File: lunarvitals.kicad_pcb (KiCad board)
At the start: 2 copper layers, 48.5 x 35 mm, 42 parts, among them J1 ConductiveCord, J2 MPU6050, J3 SEN11574, J4 MAX30102, J5 USB_C_Receptacle_PowerOnly_6P, J6 Battery, J7 Conn_01x07, Q1 FS8205, SW1 SW_SPDT, U1 NRF52840-DONGLE, U3 AP2112K-3.3, U4 TP4056, U5 MLX90614ESF-AAA-000-TU, U6 DW01A

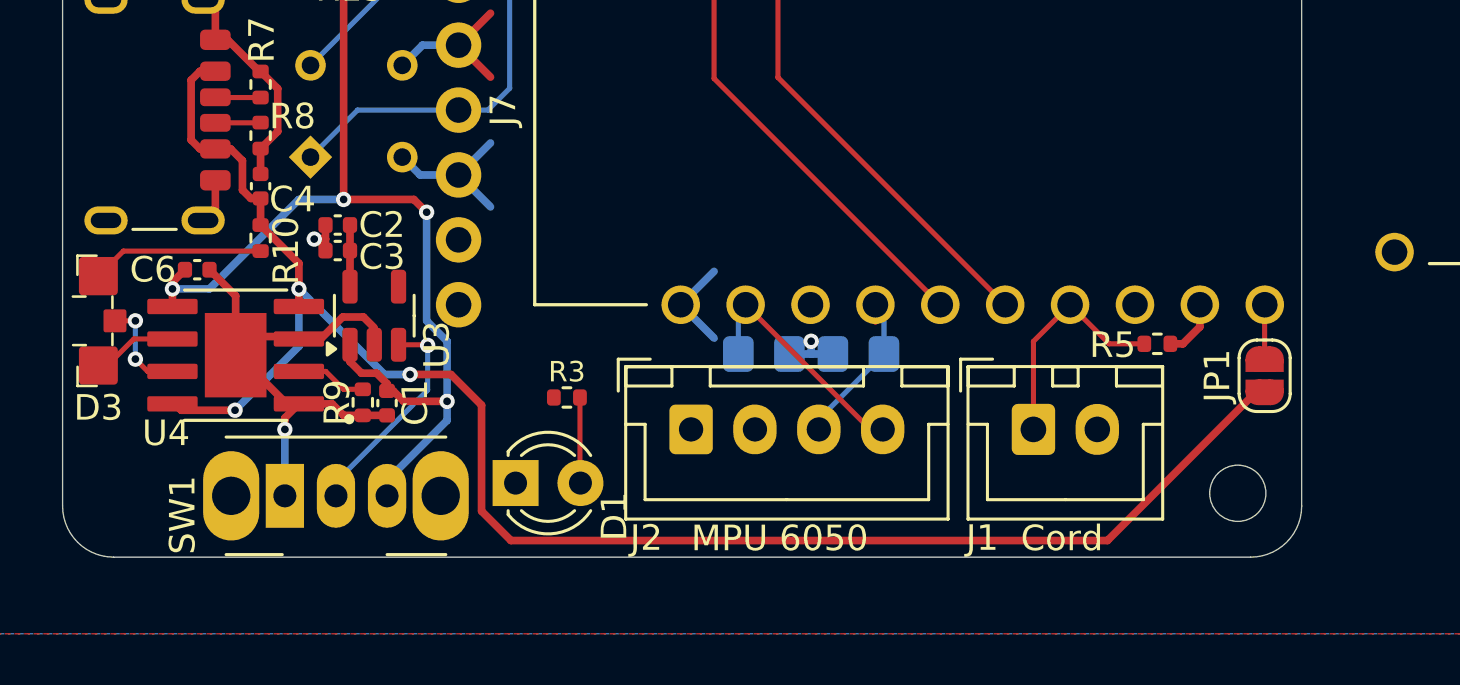
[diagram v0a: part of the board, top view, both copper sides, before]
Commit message: solder jumper pads in case of problems with various parts of the circuit
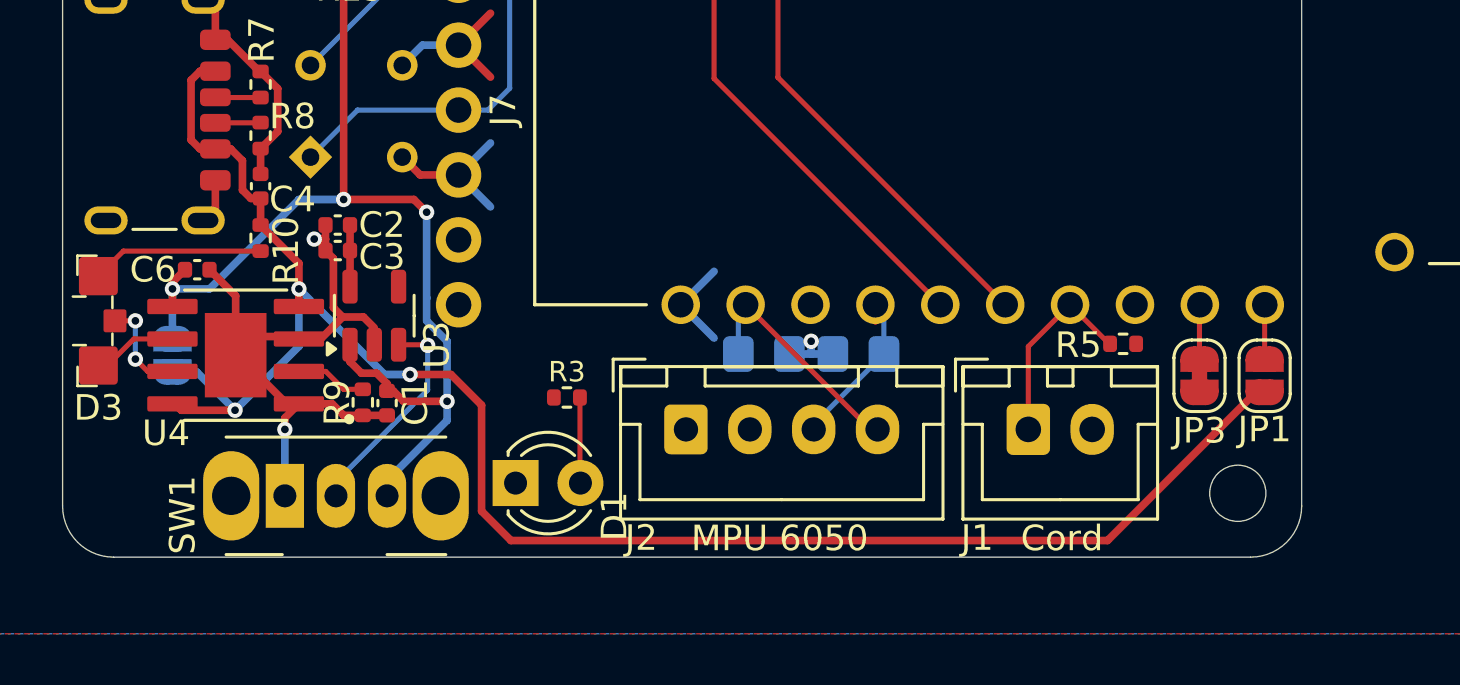
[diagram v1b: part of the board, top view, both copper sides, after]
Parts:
- added JP2: Jumper_2_Small_Open, Jumper:SolderJumper-2_P1.3mm_Open_RoundedPad1.0x1.5mm, B.Cu at (145.3, 119.6)
- added JP3: Jumper_2_Small_Bridged, Jumper:SolderJumper-2_P1.3mm_Bridged_RoundedPad1.0x1.5mm, F.Cu at (185.5, 120.4)
- moved R5 1.34 mm to (182.5, 119.2)
- moved J1 0.20 mm to (178.8, 122.5)
- moved J2 0.20 mm to (165.4, 122.5)
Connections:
- U1 pad OUT: +3.3V -> Net-(JP3-A)
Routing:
- net +5V: track 68.3 -> 71.4 mm
- net GND: track 51.4 -> 54.3 mm
- net +3.3V: track 13.3 -> 10.9 mm
- net Net-(JP3-A): track 0.00 -> 2.26 mm
- net BOut+: track 52.5 -> 54.5 mm
- net /AIN7: track 9.01 -> 7.76 mm

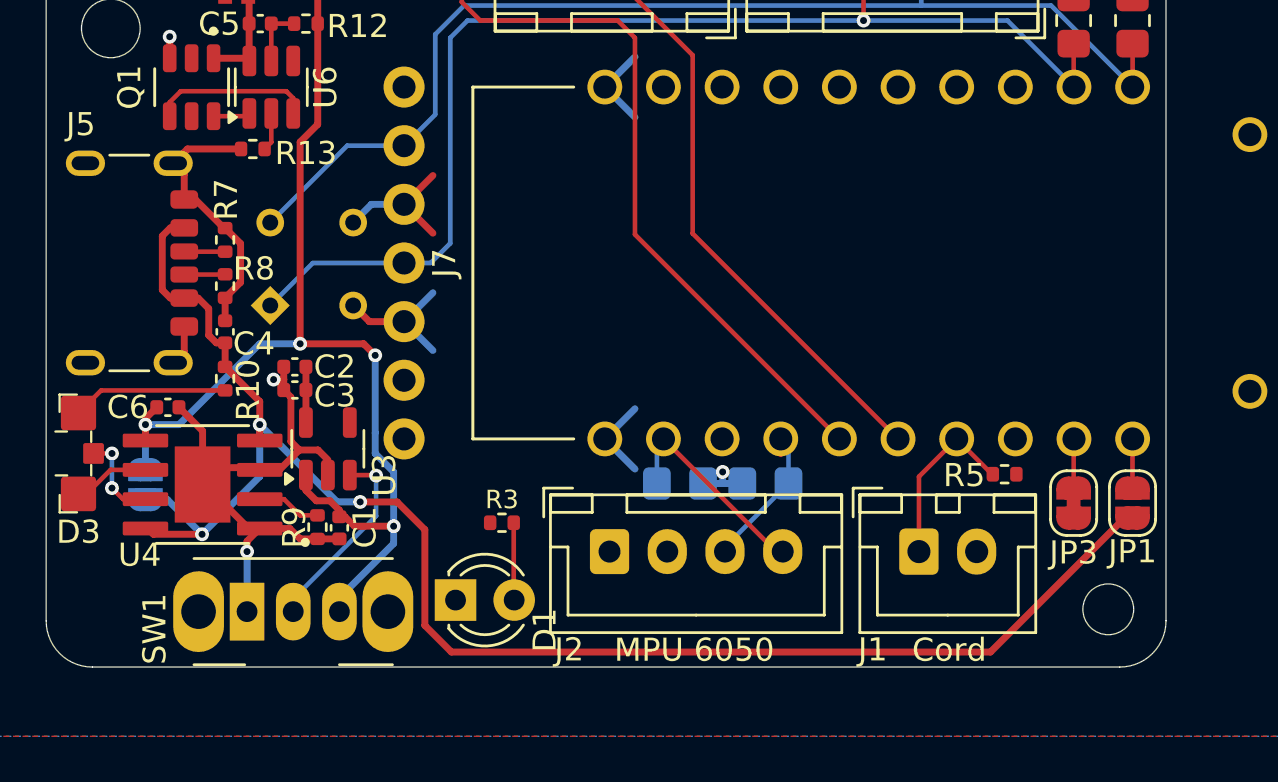
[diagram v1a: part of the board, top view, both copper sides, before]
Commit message: fix contingency solder jumper connection
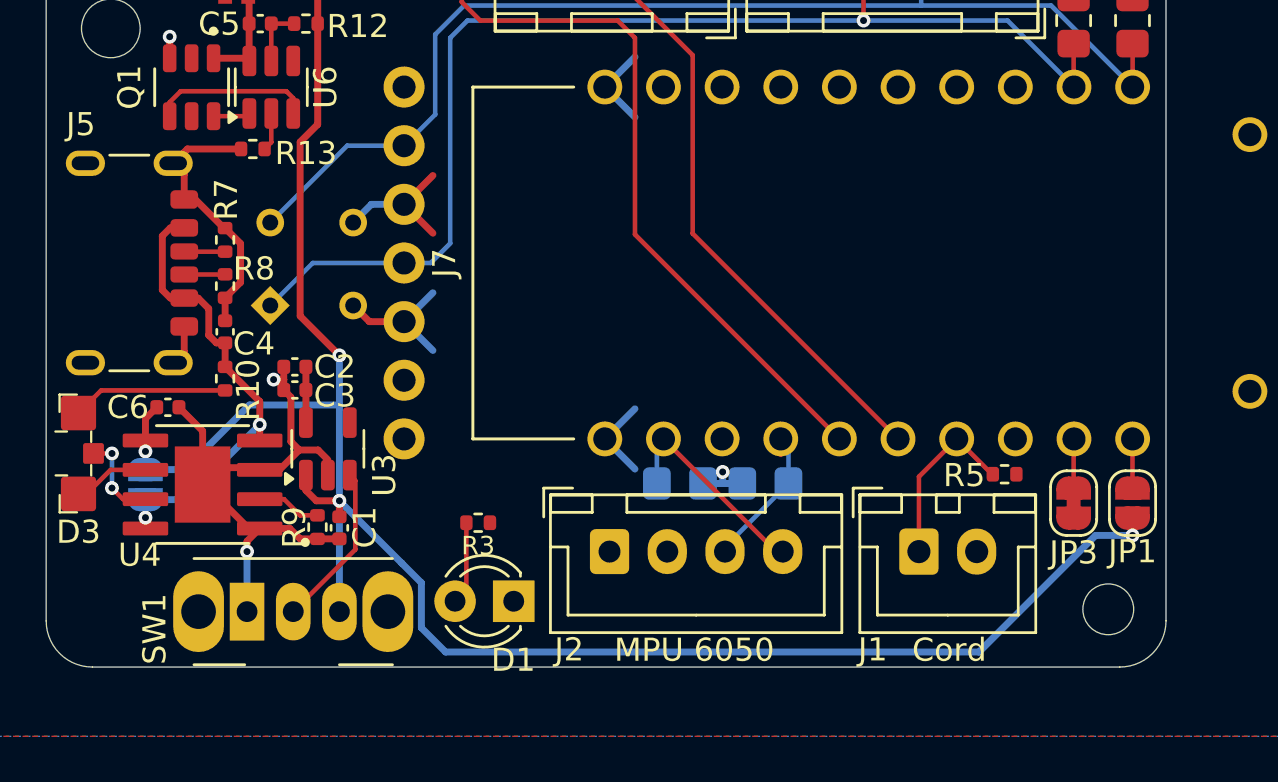
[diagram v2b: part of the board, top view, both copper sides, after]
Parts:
- moved D1 2.52 mm to (161.2, 124.7), turned to 180 degrees
- moved R3 1.03 mm to (159.7, 121.2), turned to 180 degrees
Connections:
- JP1 pad 2: +5V -> BOut+
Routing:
- net +5V: track 71.4 -> 20.7 mm, vias 3 -> 2
- net BOut+: track 54.5 -> 91.4 mm
- net Net-(SW1-B): track 8.53 -> 7.68 mm, vias 1 -> 0

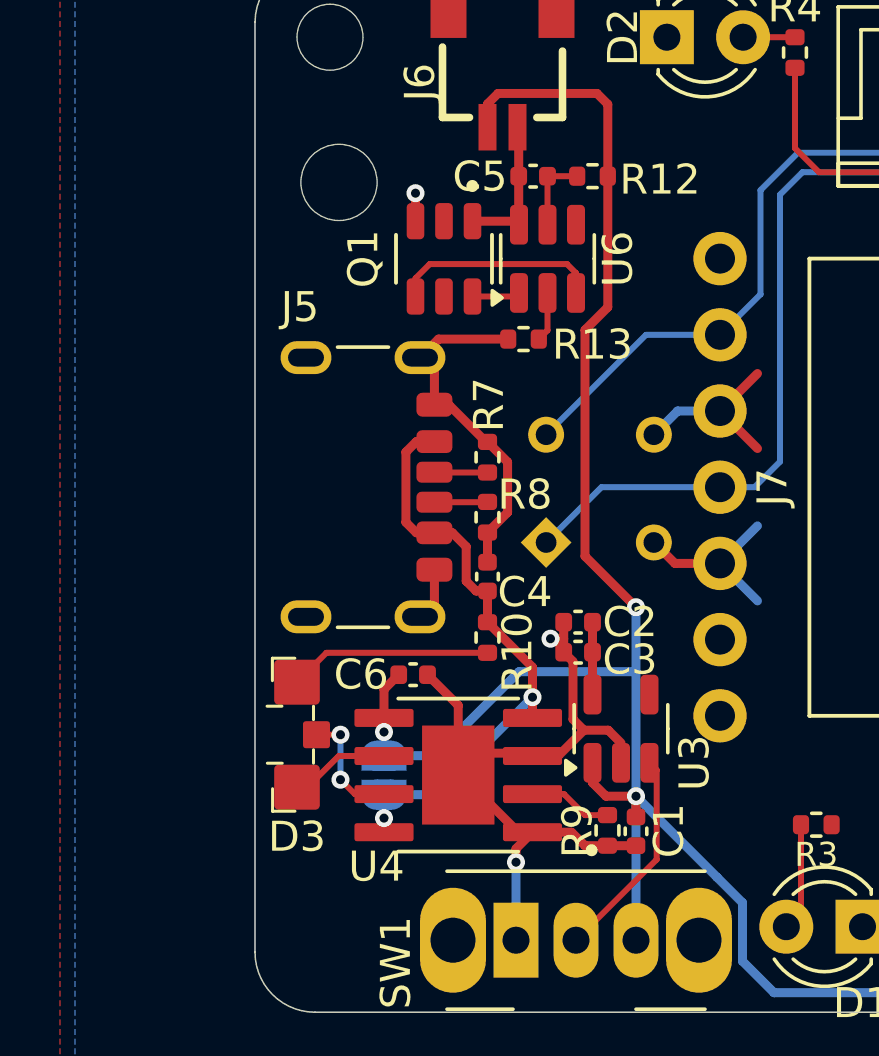
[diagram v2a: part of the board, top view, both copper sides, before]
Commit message: fix silkscreen, exclude from POS attributes
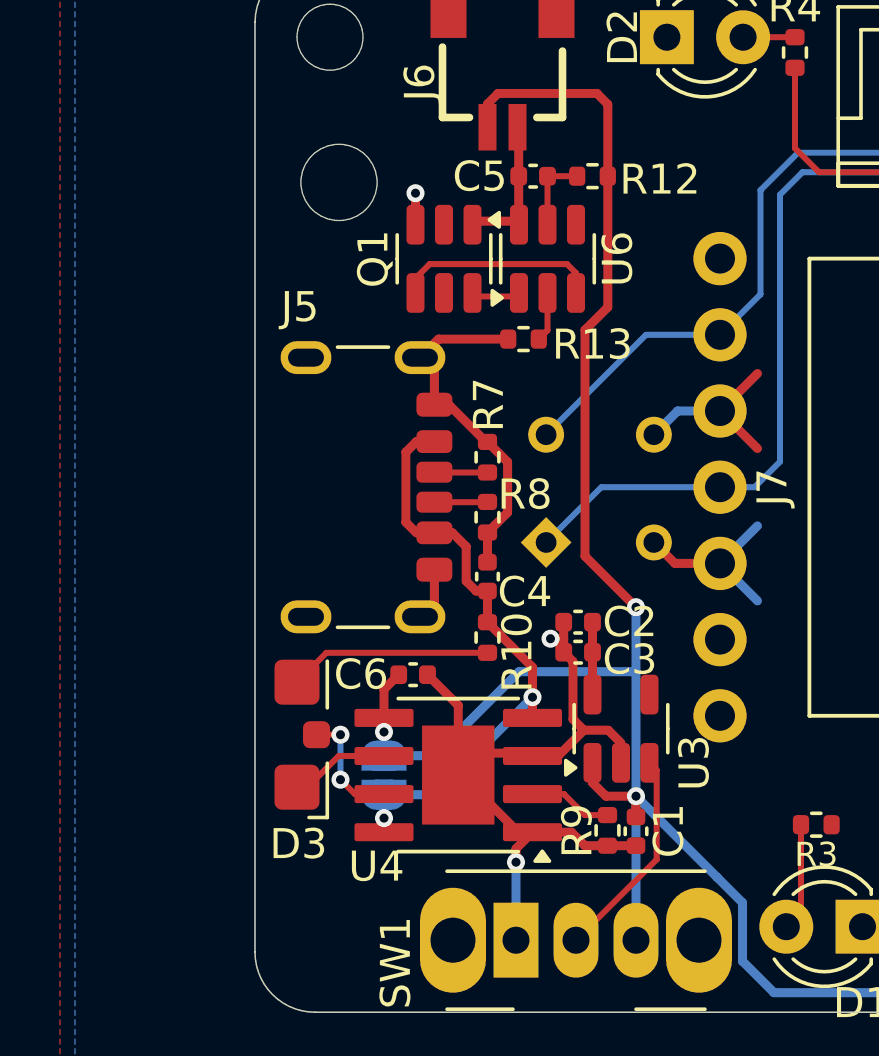
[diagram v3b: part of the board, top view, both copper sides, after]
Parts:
- D3: footprint lunar_vitals_custom:KB APBA3010SURKCGKC-GX -> LED_SMD:LED_Kingbright_KPA-3010_3x2x1mm
- Q1: footprint FS8205A:SOT95P280X145-6N -> Package_TO_SOT_SMD:SOT-23-6
- moved D3 0.50 mm to (141.9, 118.2)

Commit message: fix LED footprint
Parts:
- D3: footprint LED_SMD:LED_Kingbright_KPA-3010_3x2x1mm -> lunar_vitals_custom:LED_Kingbright_APBA3010SURKCGKC-GX_3x2x1mm
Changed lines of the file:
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@@
 		)
 	)
-	(footprint "LED_SMD:LED_Kingbright_KPA-3010_3x2x1mm"
+	(footprint "lunar_vitals_custom:LED_Kingbright_APBA3010SURKCGKC-GX_3x2x1mm"
 		(layer "F.Cu")
 		(at 141.9 118.25 90)
@@
 		(tags "Kingbright LED right-angle")
 		(property "Reference" "D3"
-			(at -3.65 0.55 180)
+			(at -3.55 0.65 180)
 			(layer "F.SilkS")
 			(effects
@@
 			)
 		)
-		(property "Footprint" "LED_SMD:LED_Kingbright_KPA-3010_3x2x1mm"
+		(property "Footprint" "lunar_vitals_custom:LED_Kingbright_APBA3010SURKCGKC-GX_3x2x1mm"
 			(at 0 0 90)
 			(unlocked yes)
@@
 		(attr smd)
 		(fp_line
-			(start -2.76 0.9)
-			(end -2.76 1.51)
+			(start 2.76 0.9)
+			(end 2.76 1.51)
 			(stroke
 				(width 0.12)
@@
 		(fp_line
 			(start 0.895 1.51)
-			(end 2.45 1.51)
+			(end 2.76 1.51)
 			(stroke
 				(width 0.12)
@@
 		)
 		(fp_line
-			(start -2.76 1.51)
+			(start -2.45 1.51)
 			(end -0.95 1.51)
 			(stroke
@@
 		)
 		(pad "1" smd roundrect
-			(at -1.75 0.5 90)
+			(at 1.75 0.5 90)
 			(size 1.5 1.5)
 			(layers "F.Cu" "F.Paste" "F.Mask")
@@
 		)
 		(pad "2" smd roundrect
-			(at 1.75 0.5 90)
-			(size 1.5 1.5)
-			(layers "F.Cu" "F.Paste" "F.Mask")
-			(roundrect_rratio 0.1666666667)
-			(net 9 "Net-(D3-K1)")
-			(pinfunction "K1")
-			(pintype "input")
-		)
-		(pad "3" smd roundrect
 			(at 0 1.15 90)
 			(size 0.9 0.9)
 			(layers "F.Cu" "F.Paste" "F.Mask")
 			(roundrect_rratio 0.25)
+			(net 9 "Net-(D3-K1)")
+			(pinfunction "K1")
+			(pintype "input")
+		)
+		(pad "3" smd roundrect
+			(at -1.75 0.5 90)
+			(size 1.5 1.5)
+			(layers "F.Cu" "F.Paste" "F.Mask")
+			(roundrect_rratio 0.1666666667)
 			(net 6 "Net-(D3-K2)")
 			(pinfunction "K2")
 			(pintype "input")
 		)
-		(model "${KICAD8_3DMODEL_DIR}/LED_SMD.3dshapes/LED_Kingbright_KPA-3010_3x2x1mm.wrl"
+		(model "${KIPRJMOD}/customlib/APBA3010-APBA3010.step"
 			(offset
-				(xyz 0 0 0)
+				(xyz 0 -0.5 0)
 			)
 			(scale
@@
 			)
 			(rotate
-				(xyz 0 0 0)
-			)
-		)
+				(xyz 0 0 180)
+			)
+		)
